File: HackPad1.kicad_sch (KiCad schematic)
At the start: 9 parts, among them SW1 SW_SPDT, U1 ATtiny85V-10P

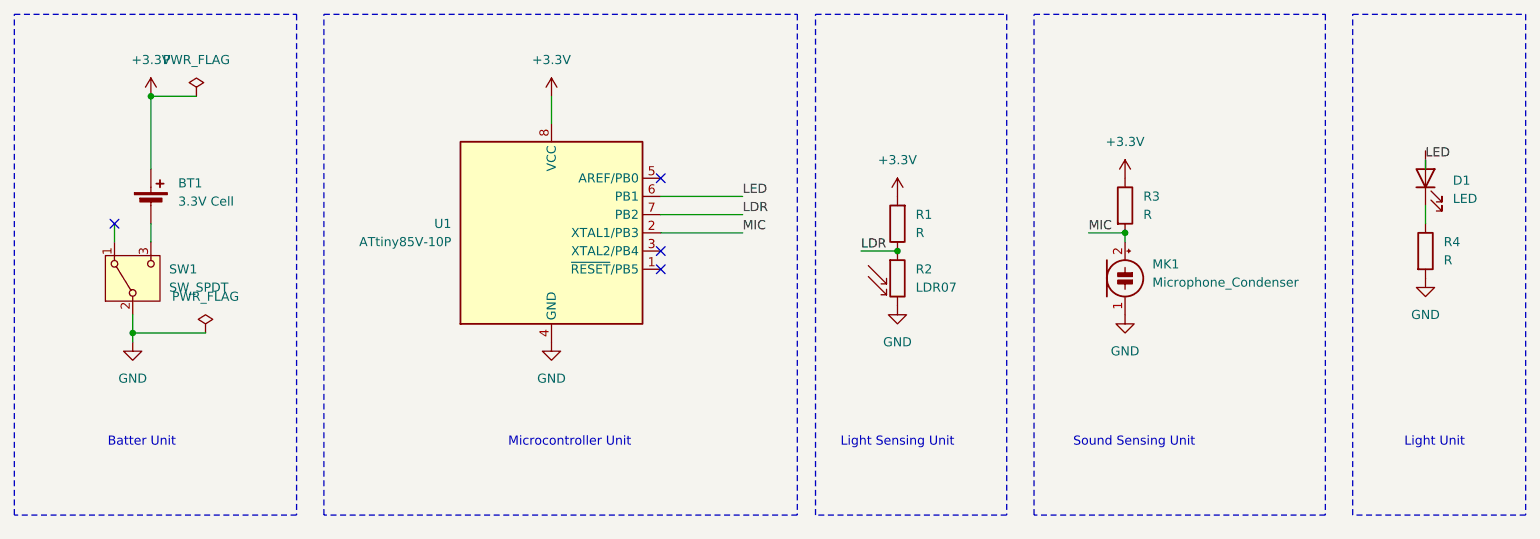
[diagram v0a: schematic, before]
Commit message: designed switch schematic
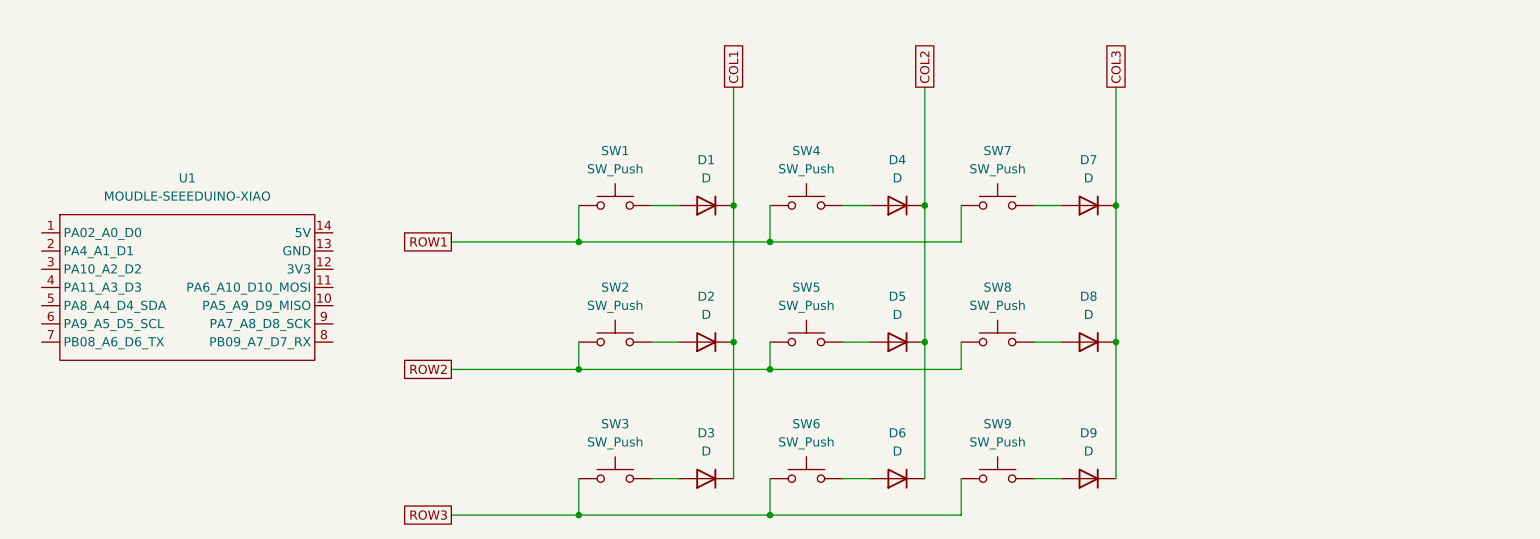
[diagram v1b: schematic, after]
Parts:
- removed BT1: 3.3V Cell, Battery:BatteryHolder_Keystone_104_1x23mm, symbol Device:Battery_Cell
- removed D1: LED, LED_THT:LED_D3.0mm_Horizontal_O1.27mm_Z2.0mm_IRGrey, symbol Device:LED
- removed MK1: Microphone_Condenser, Buzzer_Beeper:Buzzer_D14mm_H7mm_P10mm, symbol Device:Microphone_Condenser
- removed R1, R3, R4: R, Resistor_THT:R_Axial_DIN0309_L9.0mm_D3.2mm_P12.70mm_Horizontal, symbol Device:R
- removed R2: LDR07, OptoDevice:R_LDR_5.1x4.3mm_P3.4mm_Vertical, symbol Sensor_Optical:LDR07
- removed SW1: SW_SPDT, Button_Switch_SMD:Nidec_Copal_CAS-120A, symbol Switch:SW_SPDT
- removed U1: ATtiny85V-10P, Package_DIP:DIP-8_W7.62mm, symbol MCU_Microchip_ATtiny:ATtiny85V-10P
- added D1, D2, D3, D4, D5, D6, D7, D8, D9: D, symbol Device:D
- added SW1, SW2, SW3, SW4, SW5, SW6, SW7, SW8, SW9: SW_Push, symbol Switch:SW_Push
- added U1: MOUDLE-SEEEDUINO-XIAO, symbol XIAO_RP2040:MOUDLE-SEEEDUINO-XIAO
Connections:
- new net: D3.2 (A), SW3.2
- new net: D4.2 (A), SW4.2
- new net: D8.2 (A), SW8.2
- new net: D6.2 (A), SW6.2
- new net: D5.2 (A), SW5.2
- new net: D2.2 (A), SW2.2
- new net: D7.2 (A), SW7.2
- new net: D9.2 (A), SW9.2
- new net: D1.2 (A), SW1.2
- new net COL1: D1.1 (K), D2.1 (K), D3.1 (K)
- new net COL2: D4.1 (K), D5.1 (K), D6.1 (K)
- new net COL3: D7.1 (K), D8.1 (K), D9.1 (K)
- new net ROW1: SW1.1, SW4.1, SW7.1
- new net ROW2: SW2.1, SW5.1, SW8.1
- new net ROW3: SW3.1, SW6.1, SW9.1
- no-connect marks 4 -> 0
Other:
- note removed: "Batter Unit"
- note removed: "Light Sensing Unit"
- note removed: "Light Unit"
- note removed: "Microcontroller Unit"
- note removed: "Sound Sensing Unit"

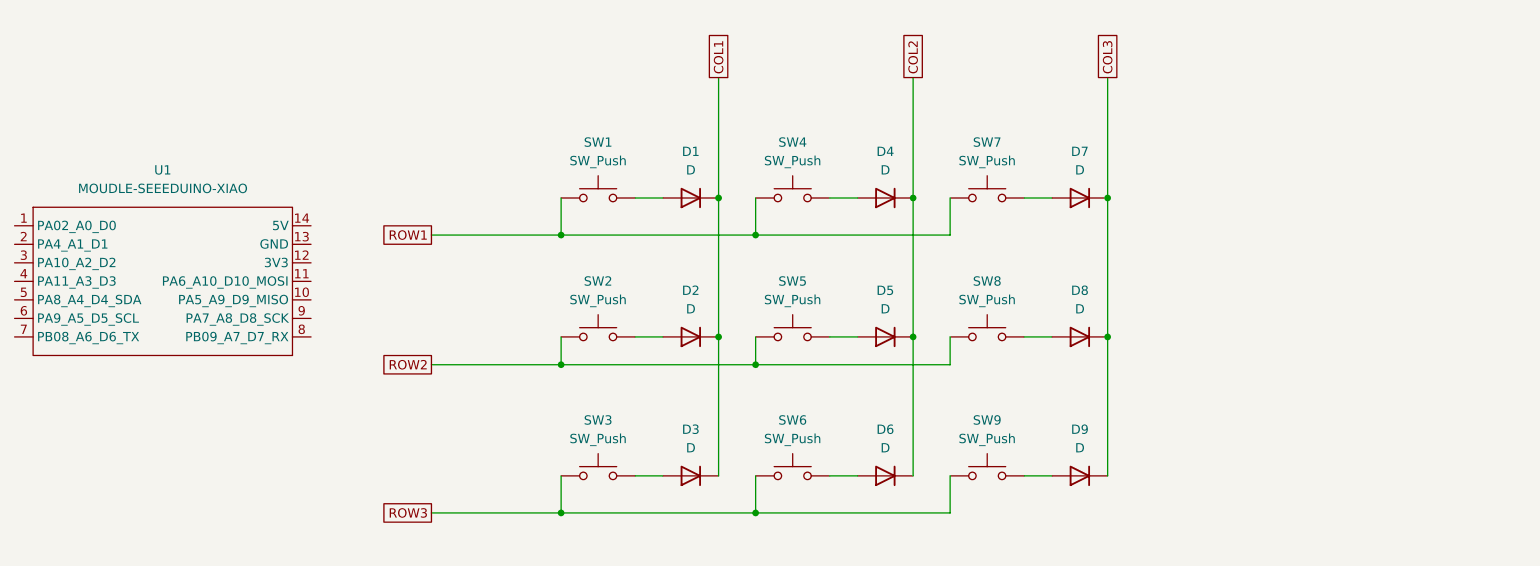
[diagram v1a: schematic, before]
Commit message: added LED schimatic
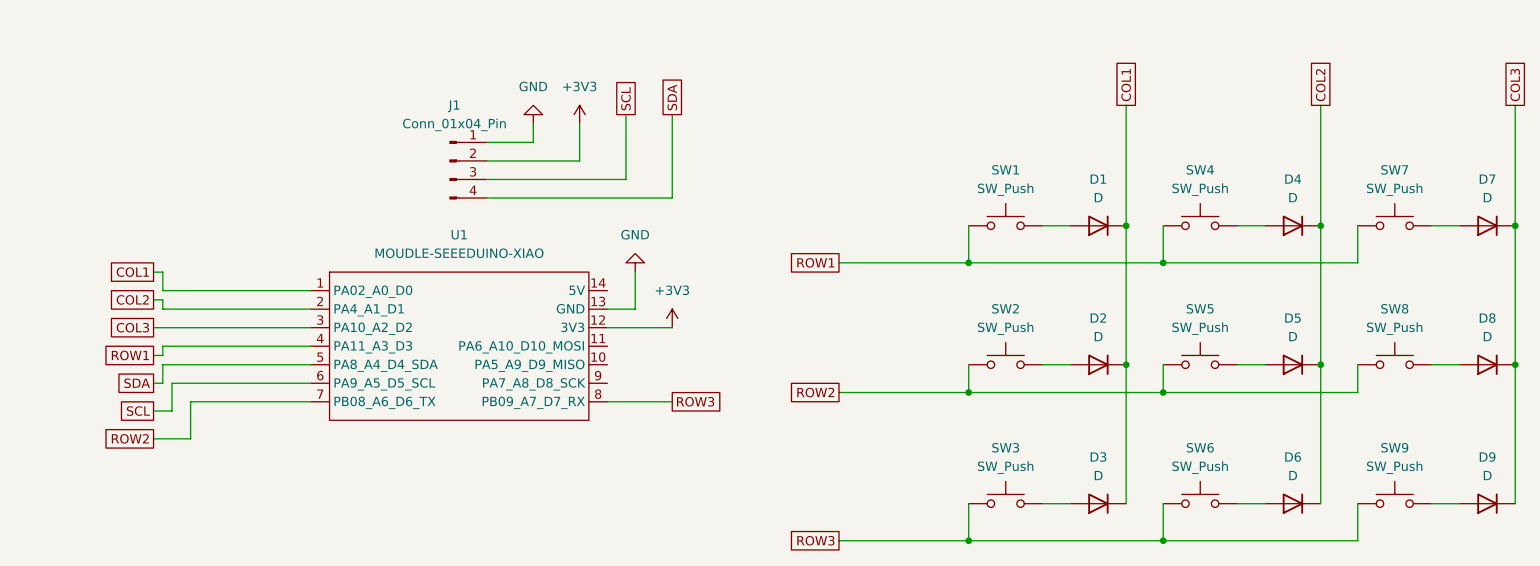
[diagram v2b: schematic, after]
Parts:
- added J1: Conn_01x04_Pin, symbol Connector:Conn_01x04_Pin
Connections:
- net COL1: now also U1.1 (PA02_A0_D0)
- net COL2: now also U1.2 (PA4_A1_D1)
- net COL3: now also U1.3 (PA10_A2_D2)
- net ROW1: now also U1.4 (PA11_A3_D3)
- net ROW2: now also U1.7 (PB08_A6_D6_TX)
- net ROW3: now also U1.8 (PB09_A7_D7_RX)
- net +3V3: now reaches U1.12 (3V3)
- net +3V3: now also J1.2 (Pin_2)
- net GND: now reaches U1.13 (GND)
- net GND: now also J1.1 (Pin_1)
- net SDA: now reaches U1.5 (PA8_A4_D4_SDA)
- net SDA: now also J1.4 (Pin_4)
- net SCL: now reaches U1.6 (PA9_A5_D5_SCL)
- net SCL: now also J1.3 (Pin_3)
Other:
- moved on the sheet: D1, D2, D3, D4, D5, D6, D7, D8, D9, SW1, SW2, SW3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

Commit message: added led schematic
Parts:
- added D10, D11, D12, D13, D14, D15, D16, D17, D18: WS2812B, LED_SMD:LED_WS2812B_PLCC4_5.0x5.0mm_P3.2mm, symbol LED:WS2812B
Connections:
- net GND: now also D10.3 (VSS), D11.3 (VSS), D12.3 (VSS), D13.3 (VSS), D14.3 (VSS), D15.3 (VSS), D16.3 (VSS), D17.3 (VSS), D18.3 (VSS)
- net LED_DATA: now reaches U1.9 (PA7_A8_D8_SCK)
- net LED_DATA: now also D10.4 (DIN)
- new net: D10.2 (DOUT), D11.4 (DIN)
- new net: D17.2 (DOUT), D18.4 (DIN)
- new net: D16.2 (DOUT), D17.4 (DIN)
- new net: D15.2 (DOUT), D16.4 (DIN)
- new net: D14.2 (DOUT), D15.4 (DIN)
- new net: D13.2 (DOUT), D14.4 (DIN)
- new net: D12.2 (DOUT), D13.4 (DIN)
- new net: D11.2 (DOUT), D12.4 (DIN)
- new net +5V: D10.1 (VDD), D11.1 (VDD), D12.1 (VDD), D13.1 (VDD), D14.1 (VDD), D15.1 (VDD), D16.1 (VDD), D17.1 (VDD), D18.1 (VDD)
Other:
- moved on the sheet: D1, D2, D3, D4, D5, D6, D7, D8, D9, J1, SW1, SW2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

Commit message: all components schematic done
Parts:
- added SW10: RotaryEncoder, symbol Device:RotaryEncoder
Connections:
- net +5V: now also U1.14 (5V)
- net GND: now also SW10.C
- net ENCA: now reaches U1.10 (PA5_A9_D9_MISO)
- net ENCA: now also SW10.A
- net ENCB: now reaches U1.11 (PA6_A10_D10_MOSI)
- net ENCB: now also SW10.B

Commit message: added footprints for diode, switch, oled
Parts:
- D1, D2, D3: footprint (none) -> Diode_THT:D_DO-35_SOD27_P7.62mm_Horizontal
- D4, D5, D6, D7, D8, D9: footprint (none) -> Diode_THT:D_DO-35_SOD27_P10.16mm_Horizontal
- J1: footprint (none) -> Connector_PinSocket_2.54mm:PinSocket_1x04_P2.54mm_Vertical
- SW1, SW2, SW3, SW4, SW5, SW6, SW7, SW8, SW9: footprint (none) -> Button_Switch_Keyboard:SW_Cherry_MX_1.00u_PCB
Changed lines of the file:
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@@
 			)
 		)
-		(property "Footprint" ""
+		(property "Footprint" "Button_Switch_Keyboard:SW_Cherry_MX_1.00u_PCB"
 			(at 142.24 85.09 0)
 			(effects
@@
 			)
 		)
-		(property "Footprint" ""
+		(property "Footprint" "Diode_THT:D_DO-35_SOD27_P7.62mm_Horizontal"
 			(at 154.94 90.17 0)
 			(effects
@@
 			)
 		)
-		(property "Footprint" ""
+		(property "Footprint" "Diode_THT:D_DO-35_SOD27_P10.16mm_Horizontal"
 			(at 181.61 52.07 0)
 			(effects
@@
 			)
 		)
-		(property "Footprint" ""
+		(property "Footprint" "Connector_PinSocket_2.54mm:PinSocket_1x04_P2.54mm_Vertical"
 			(at 40.64 26.67 0)
 			(effects
@@
 			)
 		)
-		(property "Footprint" ""
+		(property "Footprint" "Button_Switch_Keyboard:SW_Cherry_MX_1.00u_PCB"
 			(at 195.58 66.04 0)
 			(effects
@@
 			)
 		)
-		(property "Footprint" ""
+		(property "Footprint" "Diode_THT:D_DO-35_SOD27_P10.16mm_Horizontal"
 			(at 181.61 90.17 0)
 			(effects
@@
 			)
 		)
-		(property "Footprint" ""
+		(property "Footprint" "Button_Switch_Keyboard:SW_Cherry_MX_1.00u_PCB"
 			(at 168.91 66.04 0)
 			(effects
@@
 			)
 		)
-		(property "Footprint" ""
+		(property "Footprint" "Button_Switch_Keyboard:SW_Cherry_MX_1.00u_PCB"
 			(at 142.24 66.04 0)
 			(effects
@@
 			)
 		)
-		(property "Footprint" ""
+		(property "Footprint" "Button_Switch_Keyboard:SW_Cherry_MX_1.00u_PCB"
 			(at 168.91 46.99 0)
 			(effects
@@
 			)
 		)
-		(property "Footprint" ""
+		(property "Footprint" "Button_Switch_Keyboard:SW_Cherry_MX_1.00u_PCB"
 			(at 168.91 85.09 0)
 			(effects
@@
 			)
 		)
-		(property "Footprint" ""
+		(property "Footprint" "Diode_THT:D_DO-35_SOD27_P10.16mm_Horizontal"
 			(at 208.28 52.07 0)
 			(effects
@@
 			)
 		)
-		(property "Footprint" ""
+		(property "Footprint" "Button_Switch_Keyboard:SW_Cherry_MX_1.00u_PCB"
 			(at 195.58 46.99 0)
 			(effects
@@
 			)
 		)
-		(property "Footprint" ""
+		(property "Footprint" "Button_Switch_Keyboard:SW_Cherry_MX_1.00u_PCB"
 			(at 195.58 85.09 0)
 			(effects
@@
 			)
 		)
-		(property "Footprint" ""
+		(property "Footprint" "Diode_THT:D_DO-35_SOD27_P10.16mm_Horizontal"
 			(at 181.61 71.12 0)
 			(effects
@@
 			)
 		)
-		(property "Footprint" ""
+		(property "Footprint" "Diode_THT:D_DO-35_SOD27_P7.62mm_Horizontal"
 			(at 154.94 71.12 0)
 			(effects
@@
 			)
 		)
-		(property "Footprint" ""
+		(property "Footprint" "Diode_THT:D_DO-35_SOD27_P7.62mm_Horizontal"
 			(at 154.94 52.07 0)
 			(effects
@@
 			)
 		)
-		(property "Footprint" ""
+		(property "Footprint" "Diode_THT:D_DO-35_SOD27_P10.16mm_Horizontal"
 			(at 208.28 71.12 0)
 			(effects
@@
 			)
 		)
-		(property "Footprint" ""
+		(property "Footprint" "Diode_THT:D_DO-35_SOD27_P10.16mm_Horizontal"
 			(at 208.28 90.17 0)
 			(effects
@@
 			)
 		)
-		(property "Footprint" ""
+		(property "Footprint" "Button_Switch_Keyboard:SW_Cherry_MX_1.00u_PCB"
 			(at 142.24 46.99 0)
 			(effects

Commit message: added LED footprints
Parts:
- D10, D11, D12, D13, D14, D15, D16, D17, D18: footprint LED_SMD:LED_WS2812B_PLCC4_5.0x5.0mm_P3.2mm -> Keyboard_Parts:MX_SK6812MINI-E
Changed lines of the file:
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@@
 			)
 		)
-		(property "Footprint" "LED_SMD:LED_WS2812B_PLCC4_5.0x5.0mm_P3.2mm"
+		(property "Footprint" "Keyboard_Parts:MX_SK6812MINI-E"
 			(at 33.02 139.7 0)
 			(effects
@@
 			)
 		)
-		(property "Footprint" "LED_SMD:LED_WS2812B_PLCC4_5.0x5.0mm_P3.2mm"
+		(property "Footprint" "Keyboard_Parts:MX_SK6812MINI-E"
 			(at 168.275 139.7 0)
 			(effects
@@
 			)
 		)
-		(property "Footprint" "LED_SMD:LED_WS2812B_PLCC4_5.0x5.0mm_P3.2mm"
+		(property "Footprint" "Keyboard_Parts:MX_SK6812MINI-E"
 			(at 128.905 139.7 0)
 			(effects
@@
 			)
 		)
-		(property "Footprint" "LED_SMD:LED_WS2812B_PLCC4_5.0x5.0mm_P3.2mm"
+		(property "Footprint" "Keyboard_Parts:MX_SK6812MINI-E"
 			(at 90.17 139.7 0)
 			(effects
@@
 			)
 		)
-		(property "Footprint" "LED_SMD:LED_WS2812B_PLCC4_5.0x5.0mm_P3.2mm"
+		(property "Footprint" "Keyboard_Parts:MX_SK6812MINI-E"
 			(at 52.07 139.7 0)
 			(effects
@@
 			)
 		)
-		(property "Footprint" "LED_SMD:LED_WS2812B_PLCC4_5.0x5.0mm_P3.2mm"
+		(property "Footprint" "Keyboard_Parts:MX_SK6812MINI-E"
 			(at 71.12 139.7 0)
 			(effects
@@
 			)
 		)
-		(property "Footprint" "LED_SMD:LED_WS2812B_PLCC4_5.0x5.0mm_P3.2mm"
+		(property "Footprint" "Keyboard_Parts:MX_SK6812MINI-E"
 			(at 187.96 139.7 0)
 			(effects
@@
 			)
 		)
-		(property "Footprint" "LED_SMD:LED_WS2812B_PLCC4_5.0x5.0mm_P3.2mm"
+		(property "Footprint" "Keyboard_Parts:MX_SK6812MINI-E"
 			(at 148.59 139.7 0)
 			(effects
@@
 			)
 		)
-		(property "Footprint" "LED_SMD:LED_WS2812B_PLCC4_5.0x5.0mm_P3.2mm"
+		(property "Footprint" "Keyboard_Parts:MX_SK6812MINI-E"
 			(at 109.22 139.7 0)
 			(effects

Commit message: added all footprints
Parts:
- SW10: footprint (none) -> Rotary_Encoder:RotaryEncoder_Alps_EC11E-Switch_Vertical_H20mm
- U1: footprint (none) -> footprints:XIAO-Generic-Hybrid-14P-2.54-21X17.8MM
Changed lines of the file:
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@@
 			)
 		)
-		(property "Footprint" ""
+		(property "Footprint" "footprints:XIAO-Generic-Hybrid-14P-2.54-21X17.8MM"
 			(at 49.53 66.04 0)
 			(effects
@@
 			)
 		)
-		(property "Footprint" ""
+		(property "Footprint" "Rotary_Encoder:RotaryEncoder_Alps_EC11E-Switch_Vertical_H20mm"
 			(at 71.12 164.846 0)
 			(effects
